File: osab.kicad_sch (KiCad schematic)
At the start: 99 parts, among them CON1 TF-01A, CON2 PJ-3420-A-SMT, CON3 TYPE-C-31-M-12, Q1 BC847B, Q2 BC847B, SW1 PPP, SW10 RESET, SW11 Torch, SW2 VOL-, SW3 VOL+, SW4 CHAP-, SW5 CHAP+, SW6 OT/NT, SW7 BOOK-, SW8 BOOK+, SW9 BUTTON_LOCK, U1 VS1000, U2 ME6211C33M5G-N, U3 CAT25640, U4 TP4055, U5 MF5853CS, U6 PAM8302AAS, U7 MF5853CS, Y1 12MHz

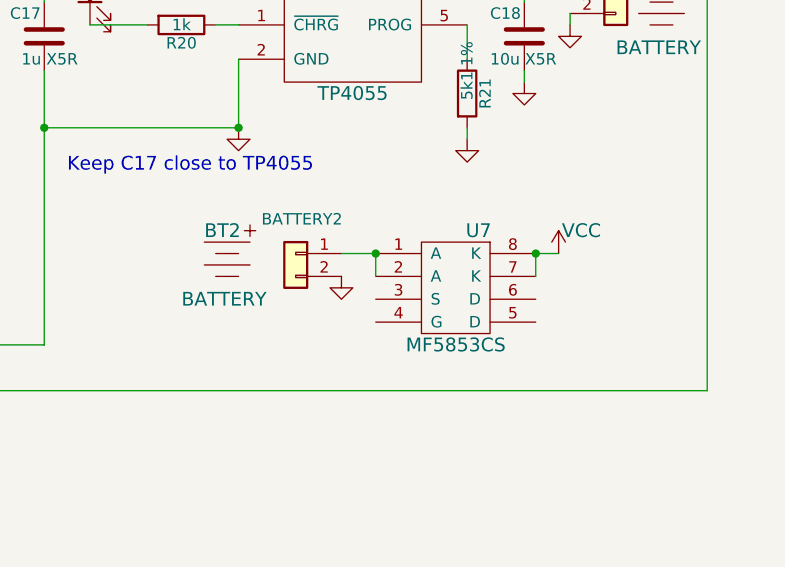
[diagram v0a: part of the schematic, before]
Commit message: production: 4.5V alkalike alternate battery
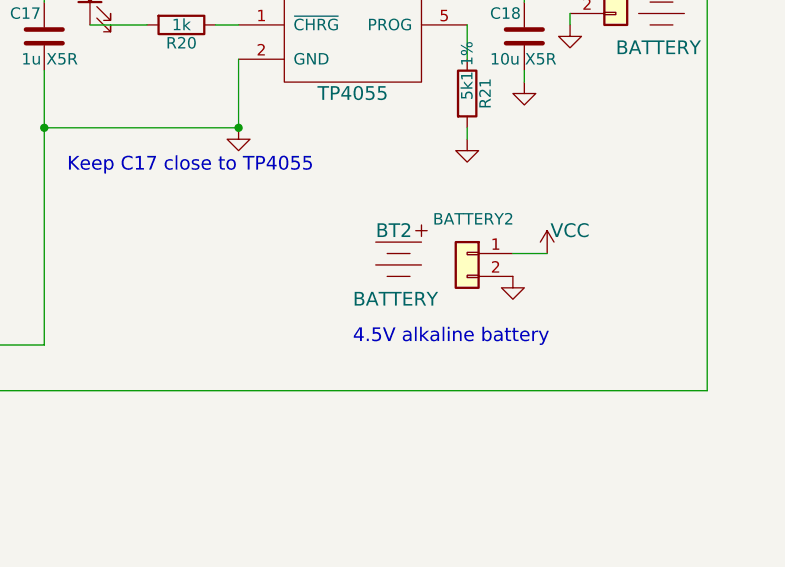
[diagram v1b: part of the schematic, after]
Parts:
- removed U7: MF5853CS, OSAB:DFN8-2x3-0.65pitch, symbol osab:PJ5853
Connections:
- net VCC: now also BATTERY2.1 (Pin_1)
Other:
- note added: "4.5V alkaline battery"
- moved on the sheet: BATTERY2, BT2
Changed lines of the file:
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@@
   (junction (at 243.84 96.52) (diameter 0) (color 0 0 0 0)
   )
-  (junction (at 242.57 147.32) (diameter 0) (color 0 0 0 0)
-  )
   (junction (at 220.98 87.63) (diameter 0) (color 0 0 0 0)
   )
@@
   (junction (at 38.1 71.12) (diameter 0) (color 0 0 0 0)
   )
-  (junction (at 260.35 147.32) (diameter 0) (color 0 0 0 0)
-  )
   (junction (at 227.33 113.03) (diameter 0) (color 0 0 0 0)
   )
@@
     (stroke (width 0) (type default) (color 0 0 0 0))
   )
-  (wire (pts (xy 238.76 147.32) (xy 242.57 147.32))
+  (wire (pts (xy 257.81 147.32) (xy 261.62 147.32))
     (stroke (width 0) (type default) (color 0 0 0 0))
   )
@@
     (stroke (width 0) (type default) (color 0 0 0 0))
   )
-  (wire (pts (xy 260.35 147.32) (xy 260.35 149.86))
-    (stroke (width 0) (type default) (color 0 0 0 0))
-  )
   (wire (pts (xy 236.22 106.68) (xy 236.22 109.22))
     (stroke (width 0) (type default) (color 0 0 0 0))
@@
     (stroke (width 0) (type default) (color 0 0 0 0))
   )
-  (wire (pts (xy 260.35 147.32) (xy 262.89 147.32))
-    (stroke (width 0) (type default) (color 0 0 0 0))
-  )
   (wire (pts (xy 76.2 73.66) (xy 43.18 73.66))
     (stroke (width 0) (type default) (color 0 0 0 0))
@@
     (stroke (width 0) (type default) (color 0 0 0 0))
   )
-  (wire (pts (xy 242.57 147.32) (xy 242.57 149.86))
-    (stroke (width 0) (type default) (color 0 0 0 0))
-  )
   (wire (pts (xy 144.78 41.91) (xy 147.32 41.91))
     (stroke (width 0) (type default) (color 0 0 0 0))
@@
     (effects (font (size 1.524 1.524)) (justify left bottom))
   )
+  (text "4.5V alkaline battery" (at 240.03 157.48 0)
+    (effects (font (size 1.524 1.524)) (justify left bottom))
+  )
   (text "Place C5 as close as possible to Vdd and Vss on CON1.\nPlace U2 as close as possible to C5.\nPlace C4 as close as possible to Vin and Vss on U2."
     (at 20.32 172.72 0)
@@
     (pin "2")
   )
-  (symbol (lib_id "Connector_Generic:Conn_01x02") (at 233.68 147.32 0) (mirror y) (unit 1)
+  (symbol (lib_id "Connector_Generic:Conn_01x02") (at 252.73 147.32 0) (mirror y) (unit 1)
     (in_bom yes) (on_board yes)
-    (property "Reference" "BATTERY2" (id 0) (at 229.87 143.51 0)
+    (property "Reference" "BATTERY2" (id 0) (at 248.92 143.51 0)
       (effects (font (size 1.27 1.27)) (justify right))
     )
-    (property "Value" "Conn_01x02" (id 1) (at 231.648 149.8346 0)
+    (property "Value" "Conn_01x02" (id 1) (at 250.698 149.8346 0)
       (effects (font (size 1.27 1.27)) (justify left) hide)
     )
-    (property "Footprint" "EasyEDA model" (id 2) (at 233.68 147.32 0)
+    (property "Footprint" "EasyEDA model" (id 2) (at 252.73 147.32 0)
       (effects (font (size 1.27 1.27)) hide)
     )
-    (property "Datasheet" "https://datasheet.lcsc.com/lcsc/2009131405_CAX-XH-2PWB_C722862.pdf" (id 3) (at 233.68 147.32 0)
+    (property "Datasheet" "https://datasheet.lcsc.com/lcsc/2009131405_CAX-XH-2PWB_C722862.pdf" (id 3) (at 252.73 147.32 0)
       (effects (font (size 1.27 1.27)) hide)
     )
-    (property "3D-model" "Included in KiCad" (id 4) (at 233.68 147.32 0)
+    (property "3D-model" "Included in KiCad" (id 4) (at 252.73 147.32 0)
       (effects (font (size 1.27 1.27)) hide)
     )
-    (property "Link" "https://lcsc.com/product-detail/Wire-To-Board-Wire-To-Wire-Connector_CAX-XH-2PWB_C722862.html" (id 5) (at 233.68 147.32 0)
+    (property "Link" "https://lcsc.com/product-detail/Wire-To-Board-Wire-To-Wire-Connector_CAX-XH-2PWB_C722862.html" (id 5) (at 252.73 147.32 0)
       (effects (font (size 1.27 1.27)) hide)
     )
-    (property "MPN" "XH-2PWB" (id 6) (at 233.68 147.32 0)
+    (property "MPN" "XH-2PWB" (id 6) (at 252.73 147.32 0)
       (effects (font (size 1.27 1.27)) hide)
     )
@@
     (pin "2")
   )
-  (symbol (lib_id "power:GND") (at 238.76 149.86 0) (unit 1)
+  (symbol (lib_id "power:GND") (at 257.81 149.86 0) (unit 1)
     (in_bom yes) (on_board yes)
-    (property "Reference" "#PWR055" (id 0) (at 238.76 156.21 0)
+    (property "Reference" "#PWR055" (id 0) (at 257.81 156.21 0)
       (effects (font (size 1.524 1.524)) hide)
     )
-    (property "Value" "GND" (id 1) (at 238.76 153.67 0)
+    (property "Value" "GND" (id 1) (at 257.81 153.67 0)
       (effects (font (size 1.524 1.524)) hide)
     )
-    (property "Footprint" "" (id 2) (at 238.76 149.86 0)
+    (property "Footprint" "" (id 2) (at 257.81 149.86 0)
       (effects (font (size 1.524 1.524)))
     )
-    (property "Datasheet" "" (id 3) (at 238.76 149.86 0)
+    (property "Datasheet" "" (id 3) (at 257.81 149.86 0)
       (effects (font (size 1.524 1.524)))
     )
@@
     (pin "3")
   )
-  (symbol (lib_id "power:VCC") (at 262.89 147.32 0) (unit 1)
+  (symbol (lib_id "power:VCC") (at 261.62 147.32 0) (unit 1)
     (in_bom yes) (on_board yes)
-    (property "Reference" "#PWR056" (id 0) (at 262.89 151.13 0)
+    (property "Reference" "#PWR056" (id 0) (at 261.62 151.13 0)
       (effects (font (size 1.524 1.524)) hide)
     )
-    (property "Value" "VCC" (id 1) (at 265.43 144.78 0)
+    (property "Value" "VCC" (id 1) (at 264.16 144.78 0)
       (effects (font (size 1.524 1.524)))
     )
-    (property "Footprint" "" (id 2) (at 262.89 147.32 0)
+    (property "Footprint" "" (id 2) (at 261.62 147.32 0)
       (effects (font (size 1.524 1.524)))
     )
-    (property "Datasheet" "" (id 3) (at 262.89 147.32 0)
+    (property "Datasheet" "" (id 3) (at 261.62 147.32 0)
       (effects (font (size 1.524 1.524)))
     )
@@
     (pin "2")
   )
-  (symbol (lib_id "osab:BATTERY") (at 226.06 143.51 0) (unit 1)
+  (symbol (lib_id "osab:BATTERY") (at 245.11 143.51 0) (unit 1)
     (in_bom yes) (on_board yes)
-    (property "Reference" "BT2" (id 0) (at 223.52 144.78 0)
+    (property "Reference" "BT2" (id 0) (at 242.57 144.78 0)
       (effects (font (size 1.524 1.524)) (justify left))
     )
-    (property "Value" "BATTERY" (id 1) (at 220.98 152.4 0)
+    (property "Value" "BATTERY" (id 1) (at 240.03 152.4 0)
       (effects (font (size 1.524 1.524)) (justify left))
     )
-    (property "Footprint" "OSAB:NULL" (id 2) (at 226.06 143.51 0)
+    (property "Footprint" "OSAB:NULL" (id 2) (at 245.11 143.51 0)
       (effects (font (size 1.524 1.524)) hide)
     )
-    (property "Datasheet" "" (id 3) (at 226.06 143.51 0)
+    (property "Datasheet" "" (id 3) (at 245.11 143.51 0)
       (effects (font (size 1.524 1.524)) hide)
     )
@@
     (pin "2")
   )
-  (symbol (lib_id "osab:PJ5853") (at 251.46 148.59 0) (unit 1)
-    (in_bom yes) (on_board yes)
-    (property "Reference" "U7" (id 0) (at 254 144.78 0)
-      (effects (font (size 1.524 1.524)))
-    )
-    (property "Value" "MF5853CS" (id 1) (at 251.46 157.48 0)
-      (effects (font (size 1.524 1.524)))
-    )
-    (property "Footprint" "OSAB:DFN8-2x3-0.65pitch" (id 2) (at 251.46 144.78 0)
-      (effects (font (size 1.524 1.524)) hide)
-    )
-    (property "Datasheet" "https://datasheet.lcsc.com/szlcsc/1910111742_Megapower-MF5853CS_C375698.pdf" (id 3) (at 251.46 144.78 0)
-      (effects (font (size 1.524 1.524)) hide)
-    )
-    (property "Link" "https://lcsc.com/product-detail/Others_Megapower-MF5853CS_C375698.html" (id 4) (at 251.46 148.59 0)
-      (effects (font (size 1.27 1.27)) hide)
-    )
-    (property "MPN" "MF5853CS" (id 5) (at 251.46 148.59 0)
-      (effects (font (size 1.27 1.27)) hide)
-    )
-    (property "3D-model" "May need to make a footprint?" (id 6) (at 251.46 148.59 0)
-      (effects (font (size 1.27 1.27)) hide)
-    )
-    (pin "1")
-    (pin "2")
-    (pin "3")
-    (pin "4")
-    (pin "5")
-    (pin "6")
-    (pin "7")
-    (pin "8")
-  )
   (symbol (lib_id "Device:R") (at 137.16 113.03 270) (unit 1)
     (in_bom yes) (on_board yes)
@@
       (reference "U6") (unit 1) (value "PAM8302AAS") (footprint "Package_SO:MSOP-8_3x3mm_P0.65mm")
     )
-    (path "/de84cf5c-224e-4bc1-ad7d-c71908826f3a"
-      (reference "U7") (unit 1) (value "MF5853CS") (footprint "OSAB:DFN8-2x3-0.65pitch")
-    )
     (path "/00000000-0000-0000-0000-00005e12ed4a"

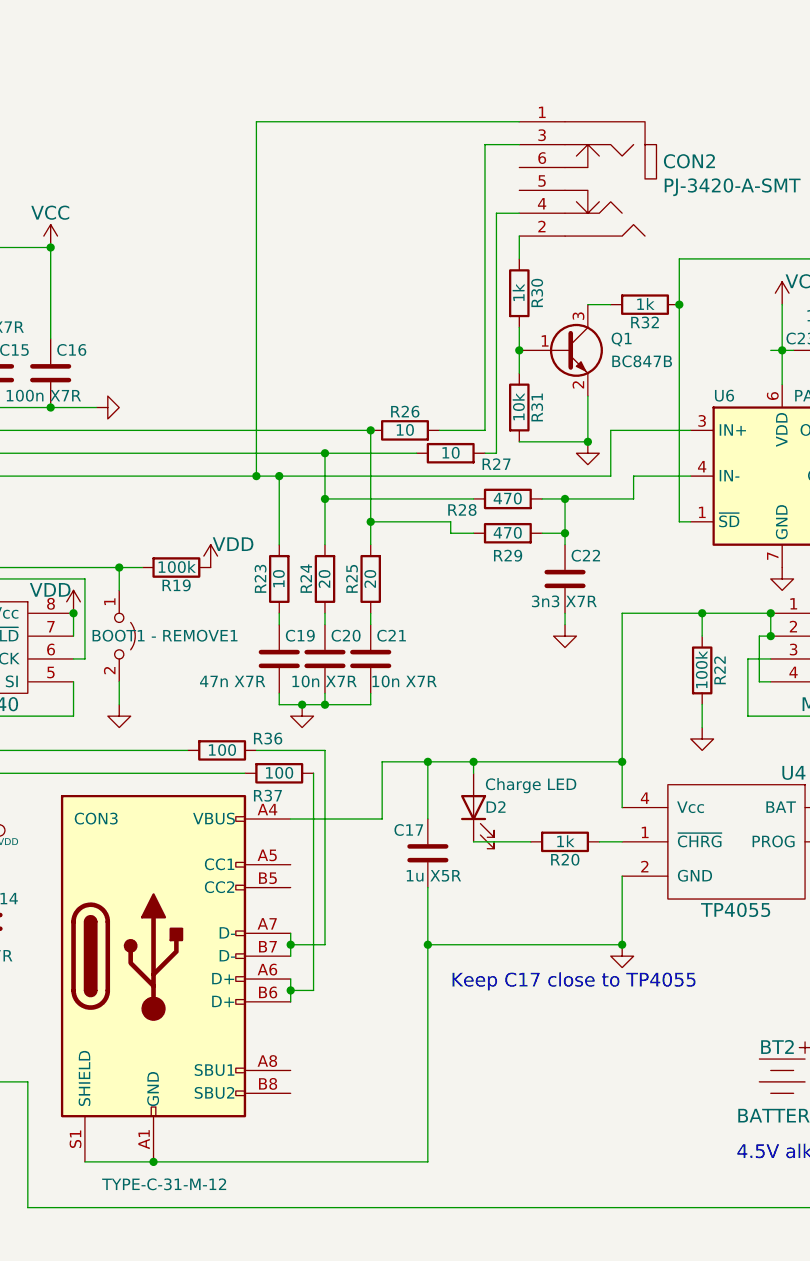
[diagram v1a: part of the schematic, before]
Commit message: production: Added CC pulldowns for USB-C and NCs where needed
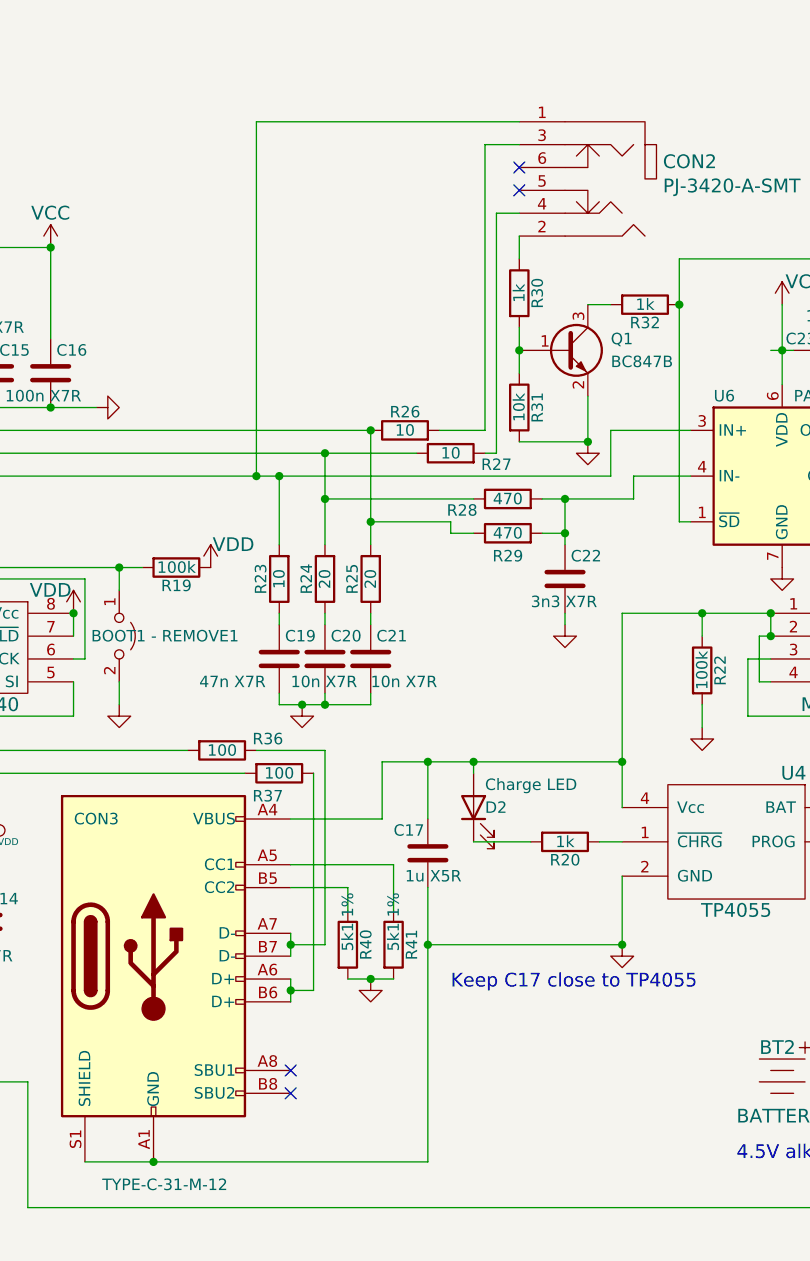
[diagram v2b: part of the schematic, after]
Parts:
- added R40, R41: 5k1 1%, Resistor_SMD:R_0603_1608Metric, symbol Device:R
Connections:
- net GND: now also R40.2, R41.2
- net at CON3.A5 (CC1): now also R41.1
- net at CON3.B5 (CC2): now also R40.1
- no-connect marks 3 -> 7
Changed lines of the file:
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@@
   (title_block
     (title "OSAB - the Open Source Audio Bible player")
-    (date "2022-03-07")
+    (date "2022-04-19")
     (rev "7")
     (company "theaudiobible.org")
@@
   (junction (at 190.5 133.35) (diameter 0) (color 0 0 0 0)
   )
+  (junction (at 199.39 137.16) (diameter 0) (color 0 0 0 0)
+  )
   (junction (at 86.36 38.1) (diameter 0) (color 0 0 0 0)
   )
@@
   (no_connect (at 44.45 110.49))
   (no_connect (at 21.59 113.03))
+  (no_connect (at 215.9 46.99))
+  (no_connect (at 215.9 49.53))
+  (no_connect (at 190.5 149.86))
+  (no_connect (at 190.5 147.32))
   (wire (pts (xy 73.66 83.82) (xy 73.66 78.74))
     (stroke (width 0) (type default) (color 0 0 0 0))
@@
     (stroke (width 0) (type default) (color 0 0 0 0))
   )
+  (wire (pts (xy 196.85 127) (xy 196.85 129.54))
+    (stroke (width 0) (type default) (color 0 0 0 0))
+  )
   (wire (pts (xy 134.62 67.31) (xy 134.62 41.91))
     (stroke (width 0) (type default) (color 0 0 0 0))
@@
     (stroke (width 0) (type default) (color 0 0 0 0))
   )
+  (wire (pts (xy 196.85 137.16) (xy 199.39 137.16))
+    (stroke (width 0) (type default) (color 0 0 0 0))
+  )
   (wire (pts (xy 53.34 93.98) (xy 58.42 93.98))
     (stroke (width 0) (type default) (color 0 0 0 0))
@@
     (stroke (width 0) (type default) (color 0 0 0 0))
   )
+  (wire (pts (xy 190.5 124.46) (xy 201.93 124.46))
+    (stroke (width 0) (type default) (color 0 0 0 0))
+  )
   (wire (pts (xy 189.23 81.28) (xy 189.23 88.9))
     (stroke (width 0) (type default) (color 0 0 0 0))
@@
     (stroke (width 0) (type default) (color 0 0 0 0))
   )
+  (wire (pts (xy 190.5 127) (xy 196.85 127))
+    (stroke (width 0) (type default) (color 0 0 0 0))
+  )
   (wire (pts (xy 212.09 76.2) (xy 212.09 44.45))
     (stroke (width 0) (type default) (color 0 0 0 0))
@@
     (stroke (width 0) (type default) (color 0 0 0 0))
   )
+  (wire (pts (xy 199.39 137.16) (xy 201.93 137.16))
+    (stroke (width 0) (type default) (color 0 0 0 0))
+  )
   (wire (pts (xy 38.1 93.98) (xy 43.18 93.98))
     (stroke (width 0) (type default) (color 0 0 0 0))
@@
     (stroke (width 0) (type default) (color 0 0 0 0))
   )
+  (wire (pts (xy 201.93 124.46) (xy 201.93 129.54))
+    (stroke (width 0) (type default) (color 0 0 0 0))
+  )
   (wire (pts (xy 76.2 73.66) (xy 43.18 73.66))
     (stroke (width 0) (type default) (color 0 0 0 0))
@@
     (pin "1")
   )
+  (symbol (lib_id "Device:R") (at 196.85 133.35 0) (unit 1)
+    (in_bom yes) (on_board yes)
+    (property "Reference" "R40" (id 0) (at 198.882 133.35 90))
+    (property "Value" "5k1 1%" (id 1) (at 196.85 130.81 90))
+    (property "Footprint" "Resistor_SMD:R_0603_1608Metric" (id 2) (at 195.072 133.35 90)
+      (effects (font (size 1.27 1.27)) hide)
+    )
+    (property "Datasheet" "https://datasheet.lcsc.com/lcsc/1811091612_Viking-Tech-ARG03FTC5101_C218090.pdf" (id 3) (at 196.85 133.35 0)
+      (effects (font (size 1.27 1.27)) hide)
+    )
+    (property "3D-model" "Included in KiCad" (id 4) (at 196.85 133.35 0)
+      (effects (font (size 1.27 1.27)) hide)
+    )
+    (property "Link" "https://lcsc.com/product-detail/Chip-Resistor-Surface-Mount_Viking-Tech-ARG03FTC5101_C218090.html" (id 5) (at 196.85 133.35 0)
+      (effects (font (size 1.27 1.27)) hide)
+    )
+    (property "MPN" "ARG03FTC5101" (id 6) (at 196.85 133.35 0)
+      (effects (font (size 1.27 1.27)) hide)
+    )
+    (pin "1")
+    (pin "2")
+  )
   (symbol (lib_id "Device:LED") (at 210.82 118.11 90) (unit 1)
     (in_bom yes) (on_board yes)
@@
     (pin "2")
   )
+  (symbol (lib_id "Device:R") (at 201.93 133.35 0) (unit 1)
+    (in_bom yes) (on_board yes)
+    (property "Reference" "R41" (id 0) (at 203.962 133.35 90))
+    (property "Value" "5k1 1%" (id 1) (at 201.93 130.81 90))
+    (property "Footprint" "Resistor_SMD:R_0603_1608Metric" (id 2) (at 200.152 133.35 90)
+      (effects (font (size 1.27 1.27)) hide)
+    )
+    (property "Datasheet" "https://datasheet.lcsc.com/lcsc/1811091612_Viking-Tech-ARG03FTC5101_C218090.pdf" (id 3) (at 201.93 133.35 0)
+      (effects (font (size 1.27 1.27)) hide)
+    )
+    (property "3D-model" "Included in KiCad" (id 4) (at 201.93 133.35 0)
+      (effects (font (size 1.27 1.27)) hide)
+    )
+    (property "Link" "https://lcsc.com/product-detail/Chip-Resistor-Surface-Mount_Viking-Tech-ARG03FTC5101_C218090.html" (id 5) (at 201.93 133.35 0)
+      (effects (font (size 1.27 1.27)) hide)
+    )
+    (property "MPN" "ARG03FTC5101" (id 6) (at 201.93 133.35 0)
+      (effects (font (size 1.27 1.27)) hide)
+    )
+    (pin "1")
+    (pin "2")
+  )
   (symbol (lib_id "power:GND") (at 120.65 190.5 0) (unit 1)
     (in_bom yes) (on_board yes)
@@
     (pin "8")
   )
+  (symbol (lib_id "power:GND") (at 199.39 137.16 0) (unit 1)
+    (in_bom yes) (on_board yes)
+    (property "Reference" "#PWR057" (id 0) (at 199.39 143.51 0)
+      (effects (font (size 1.524 1.524)) hide)
+    )
+    (property "Value" "GND" (id 1) (at 199.39 140.97 0)
+      (effects (font (size 1.524 1.524)) hide)
+    )
+    (property "Footprint" "" (id 2) (at 199.39 137.16 0)
+      (effects (font (size 1.524 1.524)))
+    )
+    (property "Datasheet" "" (id 3) (at 199.39 137.16 0)
+      (effects (font (size 1.524 1.524)))
+    )
+    (pin "1")
+  )
   (symbol (lib_id "Device:R") (at 109.22 185.42 90) (unit 1)
     (in_bom yes) (on_board yes)
@@
       (reference "#PWR056") (unit 1) (value "VCC") (footprint "")
     )
+    (path "/cc7c265c-ae9f-4b5e-ac1f-7dcc7d743aab"
+      (reference "#PWR057") (unit 1) (value "GND") (footprint "")
+    )
     (path "/00000000-0000-0000-0000-00005e19fe42"
       (reference "#PWR0101") (unit 1) (value "GND") (footprint "")
@@
       (reference "R39") (unit 1) (value "39") (footprint "Resistor_SMD:R_0603_1608Metric")
     )
+    (path "/27366f64-a3aa-46fe-899d-441ee24759e0"
+      (reference "R40") (unit 1) (value "5k1 1%") (footprint "Resistor_SMD:R_0603_1608Metric")
+    )
+    (path "/3f78dec3-05c0-40b6-97c8-31f0e399e03d"
+      (reference "R41") (unit 1) (value "5k1 1%") (footprint "Resistor_SMD:R_0603_1608Metric")
+    )
     (path "/00000000-0000-0000-0000-00005e11ca97"
